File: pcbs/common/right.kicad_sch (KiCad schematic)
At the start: 88 parts

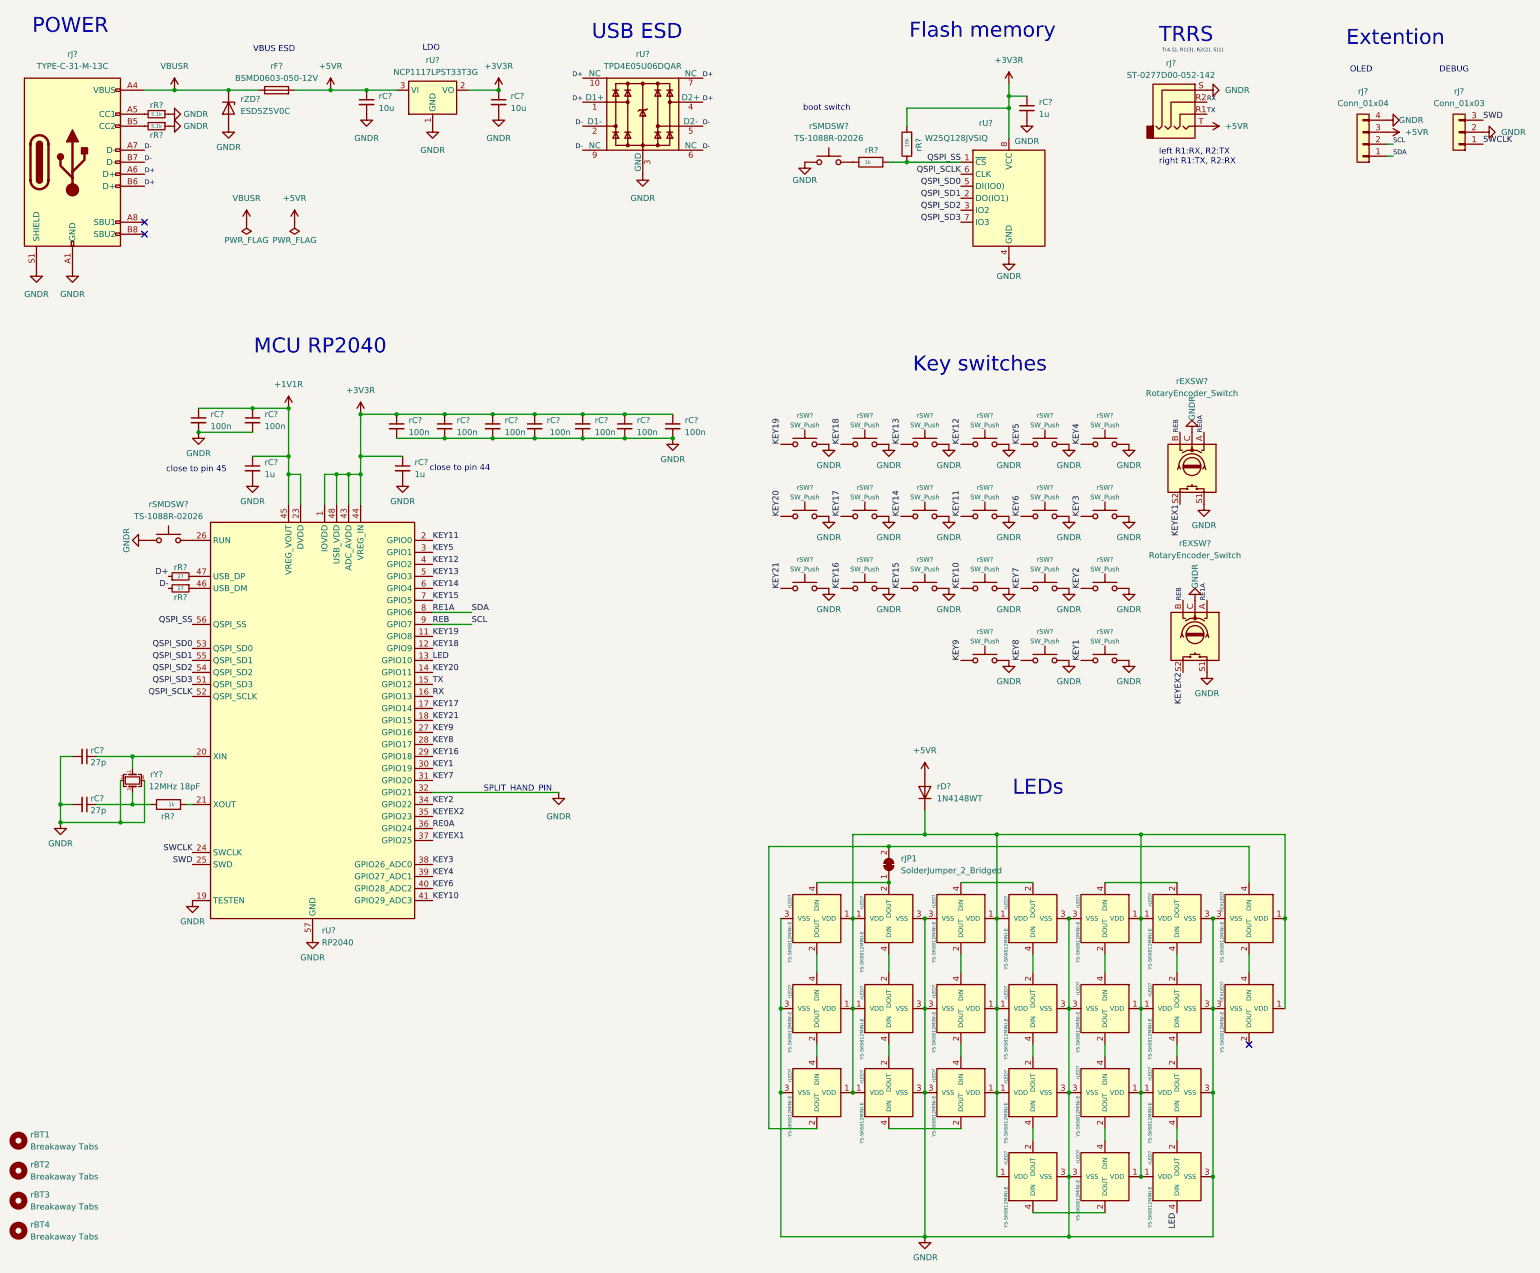
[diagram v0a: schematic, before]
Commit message: replaced trrs with USB-C
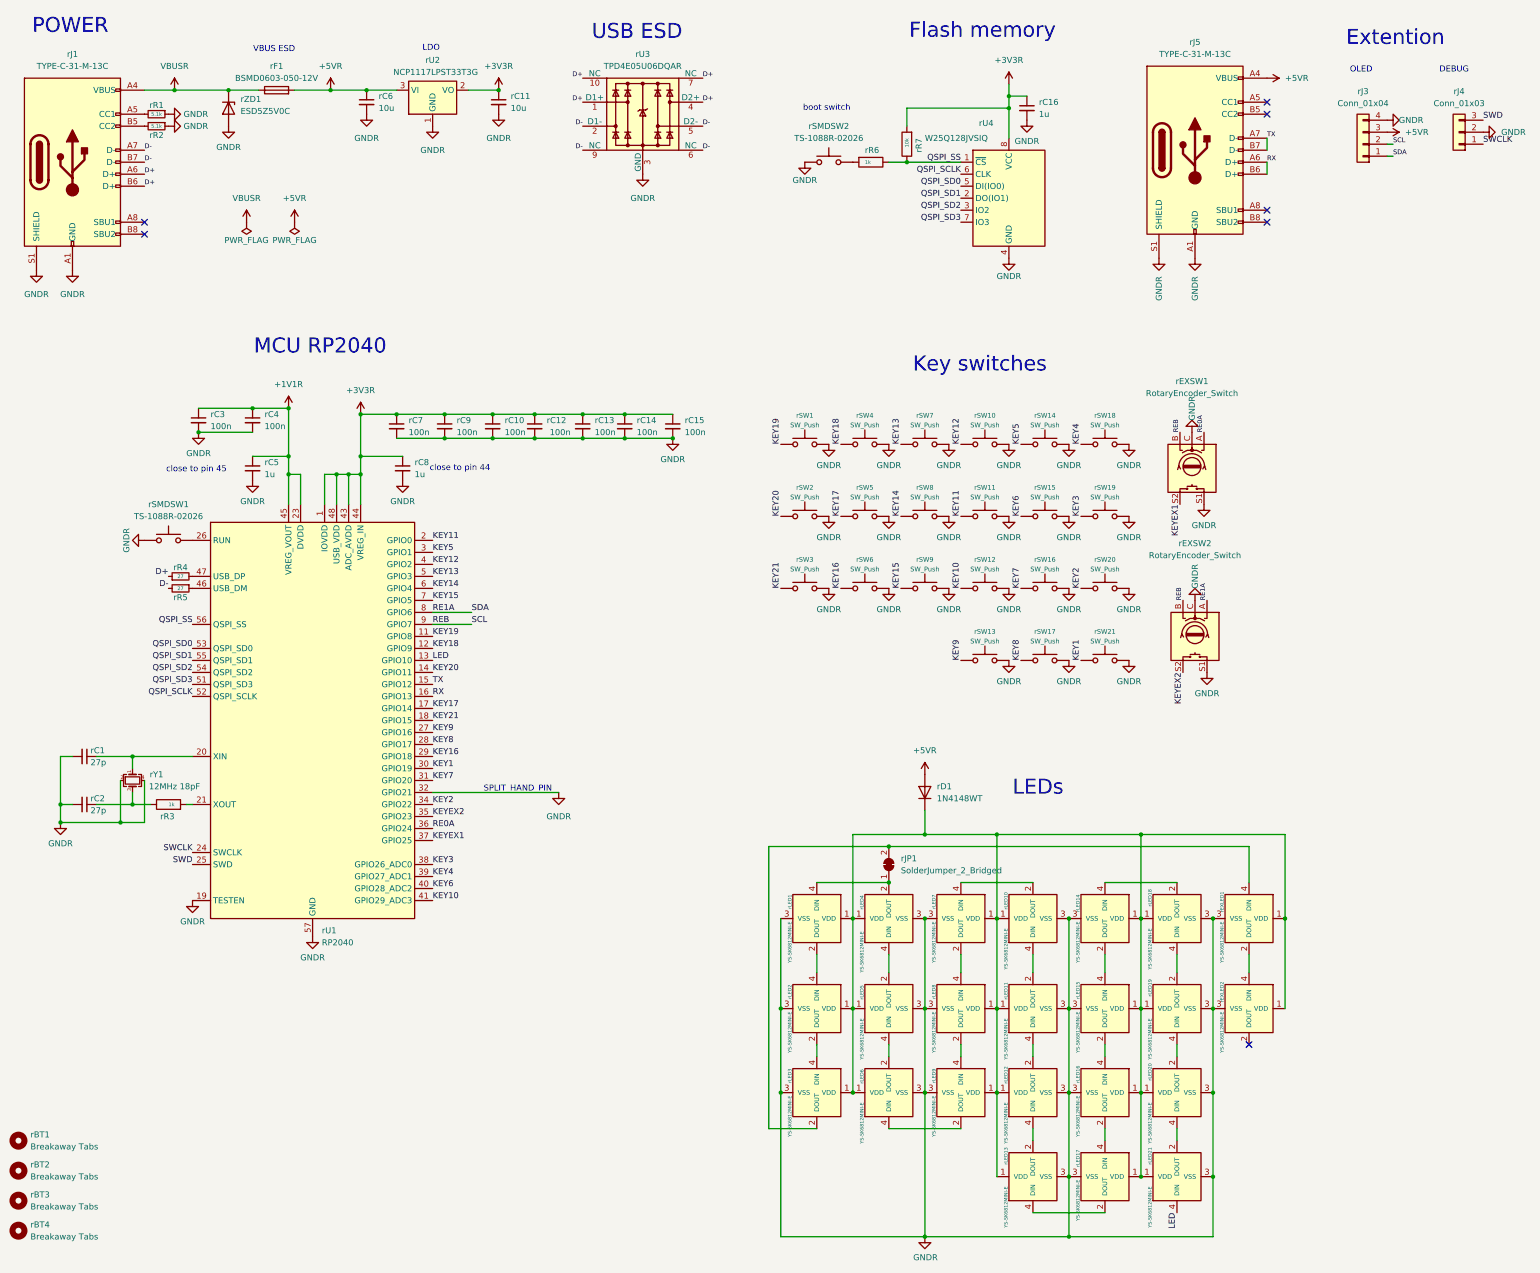
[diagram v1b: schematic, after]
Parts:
- removed rJ?: ST-0277D00-052-142, kbd_local:ST-0277D00-052-142, symbol Connector_Audio:AudioJack4
- added rJ5: TYPE-C-31-M-13C, kbd_local:TYPE-C-31-M-13C, symbol Connector:USB_C_Receptacle_USB2.0
- gave numbers to parts that had none: 82
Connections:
- net +5VR: now also rJ5.A4 (VBUS), rJ5.A9 (VBUS), rJ5.B4 (VBUS), rJ5.B9 (VBUS)
- net GNDR: now also rJ5.A1 (GND), rJ5.A12 (GND), rJ5.B1 (GND), rJ5.B12 (GND), rJ5.S1 (SHIELD)
- net RX: now also rJ5.A6 (D+), rJ5.B6 (D+)
- net TX: now also rJ5.A7 (D-), rJ5.B7 (D-)
- no-connect marks 3 -> 7
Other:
- note removed: "T(4,5), R1(3), R2(2), S(1)"
- note removed: "TRRS"
- note removed: "left R1:RX, R2:TX right R1:TX, R2:RX"
